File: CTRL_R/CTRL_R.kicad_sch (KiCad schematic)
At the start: 24 parts, among them J1 BM14B-NSHSS-TBT_LF__SN_, J2 BM04B-NSHSS-TBT_LF__SN_, J3 5051100592, U2 74LVC1G08

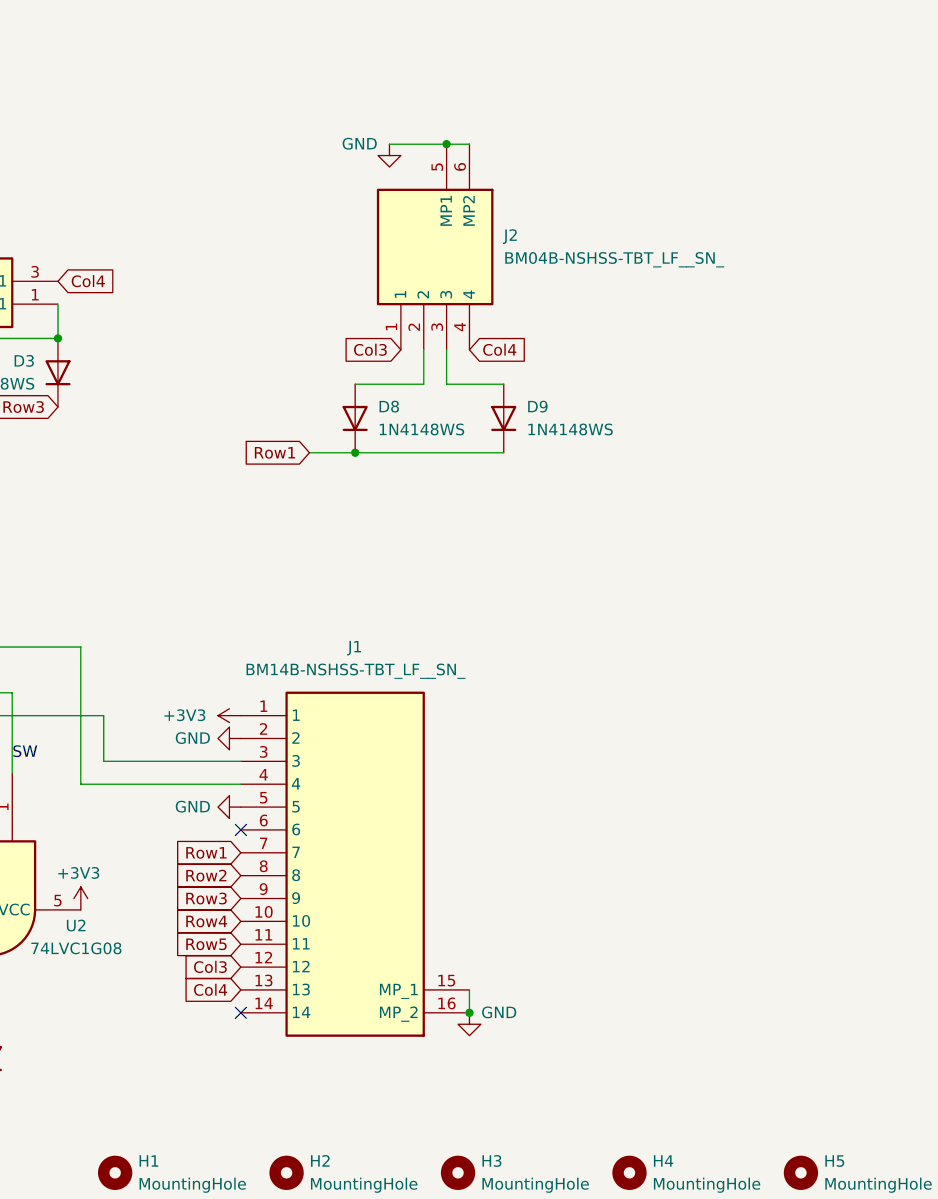
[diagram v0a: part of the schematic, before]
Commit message: CTRL Z, R, PWR Cleanup! Changes Made:
CTRL PWR -> Added Ground Plane and Ground Vias. Moved it out of parent folder CTRL_R upto Root.
CTRL Z ->  Removed Unnecessary ZX pin. Added Ground Plane and Ground Vias.
CTRL R -> Cleaned up pin count, from 14 down to 10. Added Ground Plane and Ground Vias. Made some modifications to the board shape.
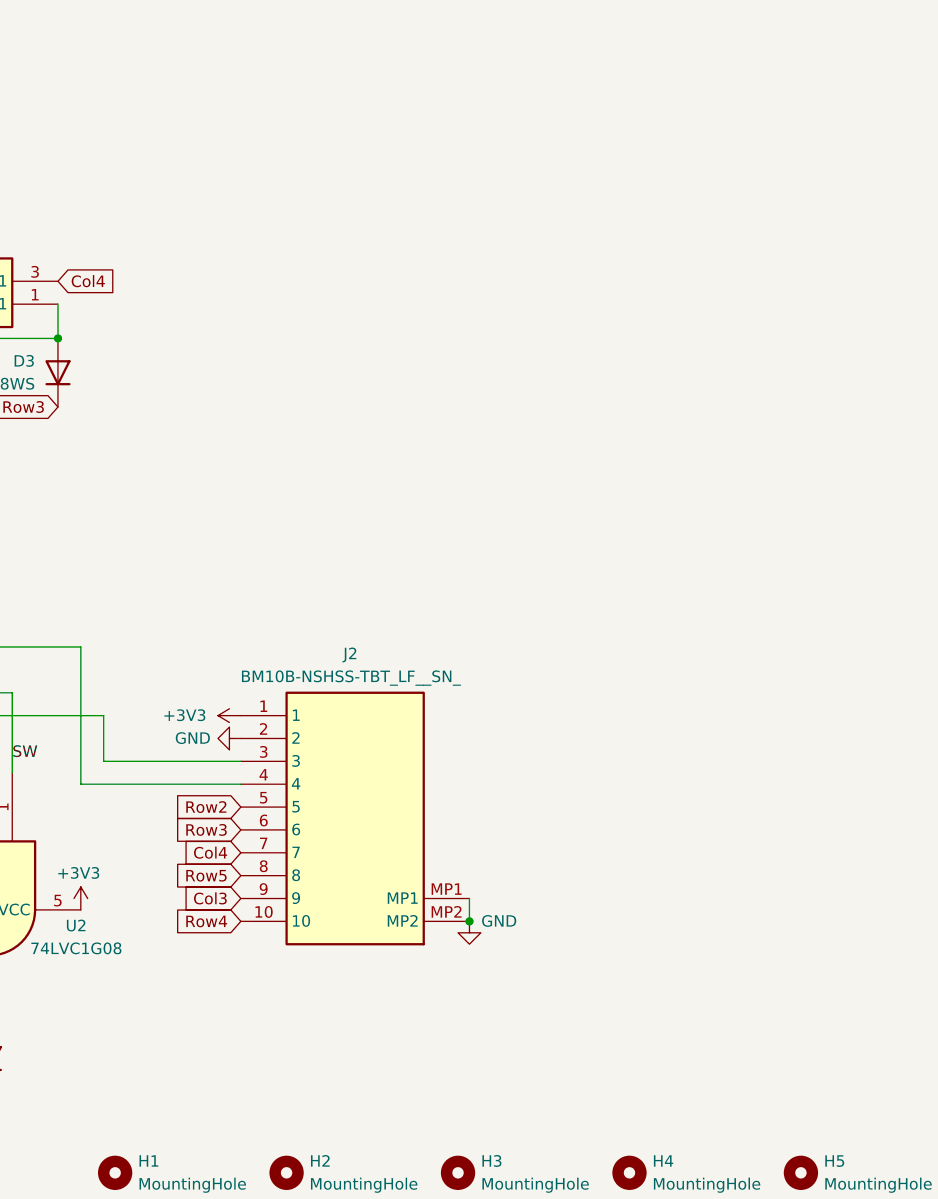
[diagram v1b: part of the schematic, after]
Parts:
- removed D8, D9: 1N4148WS, Diode_SMD:D_SOD-323, symbol Diode:1N4148WS
- removed J1: BM14B-NSHSS-TBT_LF__SN_, BM14BNSHSSTBTLFSN, symbol BM14B-NSHSS-TBT_LF__SN_:BM14B-NSHSS-TBT_LF__SN_
- removed J2: BM04B-NSHSS-TBT_LF__SN_, BM04B-NSHSS-TBT:BM04BNSHSSTBTLFSN, symbol BM04B-NSHSS-TBT_LF__SN_:BM04B-NSHSS-TBT_LF__SN_
- added J2: BM10B-NSHSS-TBT_LF__SN_, BM10BNSHSSTBTLFSN, symbol BM10B-NSHSS-TBT_LF__SN_:BM10B-NSHSS-TBT_LF__SN_
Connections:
- net +3V3: now also J2.1
- net ADC_X: now also J2.3
- net ADC_Y: now also J2.4
- net Col3: now also J2.9
- net Col4: now also J2.7
- net GND: now also J2.2, J2.MP1, J2.MP2
- net Row2: now also J2.5
- net Row3: now also J2.6
- net Row4: now also J2.10
- net Row5: now also J2.8
- no-connect marks 2 -> 0

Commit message: Updated CTRL_Z to use 3 pin FPC and ESD Protection.
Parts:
- removed J2: BM10B-NSHSS-TBT_LF__SN_, BM10BNSHSSTBTLFSN, symbol BM10B-NSHSS-TBT_LF__SN_:BM10B-NSHSS-TBT_LF__SN_
- added J1: 5034801400, 5034801400:5034801400, symbol 5034801400:5034801400
- added J2: 503480-0440, 5034800440, symbol 503480-0440:503480-0440
- added U1: DRV5033FAxDBZ, Package_TO_SOT_SMD:SOT-23, symbol Sensor_Magnetic:DRV5033FAxDBZ
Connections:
- net +3V3: now also J1.3, U1.1 (VCC)
- net ADC_X: now also J1.5
- net ADC_Y: now also J1.6
- net Col3: now also J1.11
- net Col4: now also J1.9
- net GND: now also J1.13, J1.4, J1.P1, J1.P2, U1.3 (GND)
- net Row2: now also J1.7
- net Row3: now also J1.8
- net Row4: now also J1.12
- net Row5: now also J1.10
- new net HALL: J1.1, U1.2 (OUT)
- new net Row1: J1.2
- new net SL_BRI: J1.14

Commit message: Updated CTRL_R to have ESD diodes, CTRL_Z connector, FPC, yada yada.
Its the same stuff as the commit with CTRL_L.
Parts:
- removed H1, H2, H3, H4, H5: MountingHole, MountingHole:MountingHole_2.7mm_M2.5, symbol Mechanical:MountingHole
- removed J2: 503480-0440, 5034800440, symbol 503480-0440:503480-0440
- added D23, D24, D25, D26, D27, D28, D29, D30, D31: ESD5V0B03, A_HDJ_Library:D_0402_1005Metric, symbol Diode:ESD9B5.0ST5G
- added H6, H7, H8, H9: MountingHole_Pad, MountingHole:MountingHole_2.7mm_M2.5_Pad, symbol Mechanical:MountingHole_Pad
- added J2, J6: AYF530365TA, AYF530365TA:AYF530365T, symbol AYF530365TA:AYF530365TA
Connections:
- net +3V3: now also J1.12; no longer J1.3
- net ADC_X: now also J1.10; no longer J1.5
- net ADC_Y: now also J1.9; no longer J1.6
- net Col3: now also J1.4, D30.2 (A2), J6.3; no longer J1.11
- net Col4: now also J1.6, D29.2 (A2), J6.1; no longer J1.9
- net GND: now also J1.11, D23.1 (A1), D24.1 (A1), D25.1 (A1), D26.1 (A1), D27.1 (A1), D28.1 (A1), D29.1 (A1), D30.1 (A1), D31.1 (A1), H6.1, H7.1, H8.1, H9.1, J2.3, J2.4 (MP1), J2.5 (MP2), J6.4 (MP1), J6.5 (MP2); no longer J1.13, J1.4
- net HALL: now also J1.14; no longer J1.1
- net Row1: now also J1.13, J6.2; no longer J1.2
- net Row2: now also J1.8; no longer J1.7
- net Row3: now also J1.7; no longer J1.8
- net Row4: now also J1.3; no longer J1.12
- net Row5: now also J1.5; no longer J1.10
- net SL_BRI: now also J1.1, J2.2; no longer J1.14
- net at D7.2 (A), U2.4: now also D31.2 (A2)
- net at D3.2 (A), S3.1 (COM_1), S3.2 (COM_2): now also D26.2 (A2)
- net at D6.2 (A), S6.1 (COM_1), S6.2 (COM_2): now also D24.2 (A2)
- net at D2.2 (A), S2.1 (COM_1), S2.2 (COM_2): now also D27.2 (A2)
- net at D4.2 (A), S4.1 (COM_1), S4.2 (COM_2): now also D25.2 (A2)
- net at D1.2 (A), S1.1 (COM_1), S1.2 (COM_2): now also D28.2 (A2)
- net at D5.2 (A), S5.1 (COM_1), S5.2 (COM_2): now also D23.2 (A2)
- new net SL_VIN: J1.2, J2.1
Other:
- moved on the sheet: D7, J1

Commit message: Updated CTRL_R to use 4 pin FPC and fixed DRC errors.
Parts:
- removed J3: 5051100592, 5051100592:CON_5051100592_MOL, symbol 5051100592:5051100592
- removed J6: AYF530365TA, AYF530365TA:AYF530365T, symbol AYF530365TA:AYF530365TA
- added J4: 503480-0440, 5034800440, symbol 503480-0440:503480-0440
- added J5: 503480-0540, 503480-0540:5034800540, symbol 503480-0540:503480-0540
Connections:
- net +3V3: now also J5.5
- net ADC_X: now also J5.4
- net ADC_Y: now also J5.1
- net Col3: now also J4.3
- net Col4: now also J4.1
- net GND: now also J4.4, J4.MP1, J4.MP2, J5.2, J5.MP1, J5.MP2
- net Row1: now also J4.2
- net SW: now also J5.3

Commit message: Multiplexed Debug HDMI port with DDIB screen, there are no BIOS versions with HDMI out on TCP1.
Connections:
- net ADC_X: now also J1.9, J5.1; no longer J1.10, J5.4
- net ADC_Y: now also J1.10, J5.4; no longer J1.9, J5.1
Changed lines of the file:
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@@
 		)
 	)
-	(label "ADC_X"
+	(label "ADC_Y"
 		(at 102.87 95.25 0)
 		(effects
@@
 		)
 	)
-	(label "ADC_Y"
+	(label "ADC_X"
 		(at 102.87 87.63 0)
 		(effects

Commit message: Updated CTRLs to be one sided (saves a billion dollars somehow), added LCSC_Parts for BOM, and other fixes. (Part 1/2)
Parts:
- D1, D2, D3, D4, D5, D6, D7: LCSC Part (none) -> C917117
- H6, H7, H8, H9: LCSC Part (none) -> N/A
- J1: LCSC Part (none) -> C505360
- J2: LCSC Part (none) -> C5571510
- J4: LCSC Part (none) -> C3170007
- J5: LCSC Part (none) -> C5527934
- S1, S2, S3, S4, S5, S6: LCSC Part (none) -> C2733655
- U1: LCSC Part (none) -> C2869057
- U2: LCSC Part (none) -> C53185136
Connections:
- net +3V3: now also J5.1; no longer J5.5
- net ADC_X: now also J5.5; no longer J5.1
- net ADC_Y: now also J5.2; no longer J5.4
- net Col3: now also J4.2; no longer J4.3
- net Col4: now also J4.4; no longer J4.1
- net GND: now also J4.1, J5.4; no longer J4.4, J5.2
- net Row1: now also J4.3; no longer J4.2

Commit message: Created updated BOM for PCBWay on all CTRL daughterboards. These boards have likely hit their final* version
*Ive said "Finished Version" many times in this project. I'm confident now, but no guarantees.
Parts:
- D1, D2, D3, D4, D5, D6, D7: MPN (none) -> 1N4148WS; Manufacturer (none) -> JSMSEMI
- D23, D24, D25, D26, D27, D28, D29, D30, D31: MPN (none) -> ESD5V0B03-1006; Manufacturer (none) -> TECH PUBLIC
- J1: MPN (none) -> 5034801400; Manufacturer (none) -> MOLEX
- J2: MPN (none) -> AYF530365TA; Manufacturer (none) -> PANASONIC
- J4: MPN (none) -> 5034800440; Manufacturer (none) -> MOLEX
- J5: MPN (none) -> 5034800540; Manufacturer (none) -> MOLEX
- S1, S2, S3, S4, S5, S6: MPN (none) -> B3S-1000; Manufacturer (none) -> OMRON
- U1: MPN (none) -> DRV5033FAQDBZR; Manufacturer (none) -> TI
- U2: MPN (none) -> 74LVC1G08GV; Manufacturer (none) -> MDD(Microdiode Semiconductor)
